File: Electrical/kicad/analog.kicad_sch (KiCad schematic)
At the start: 2 parts, among them IC2 PCM1795DBR

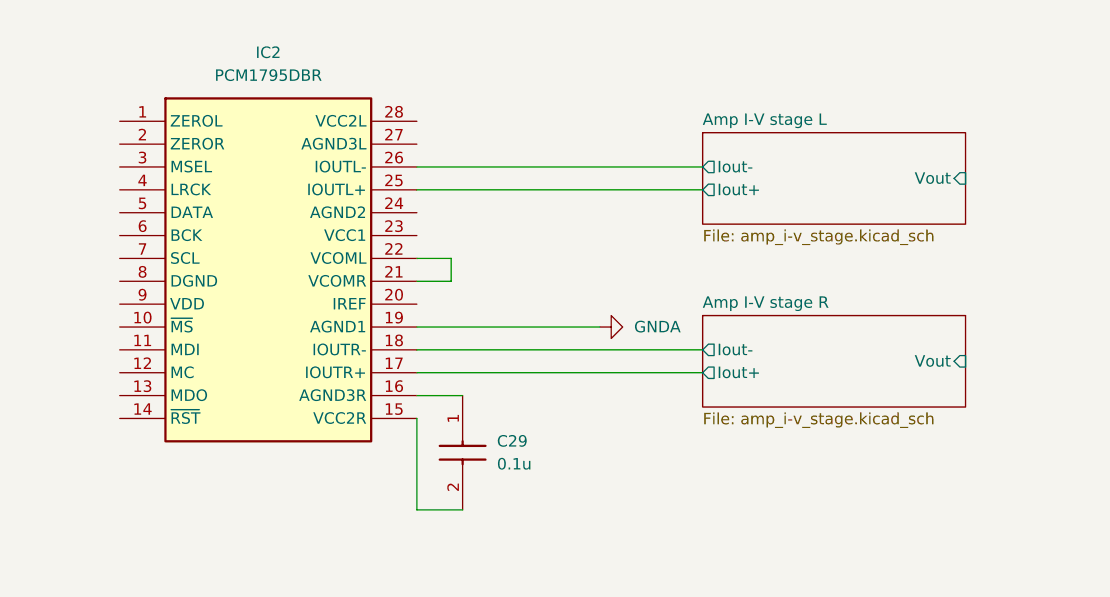
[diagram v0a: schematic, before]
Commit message: Updated PCM1795 schematic sheet
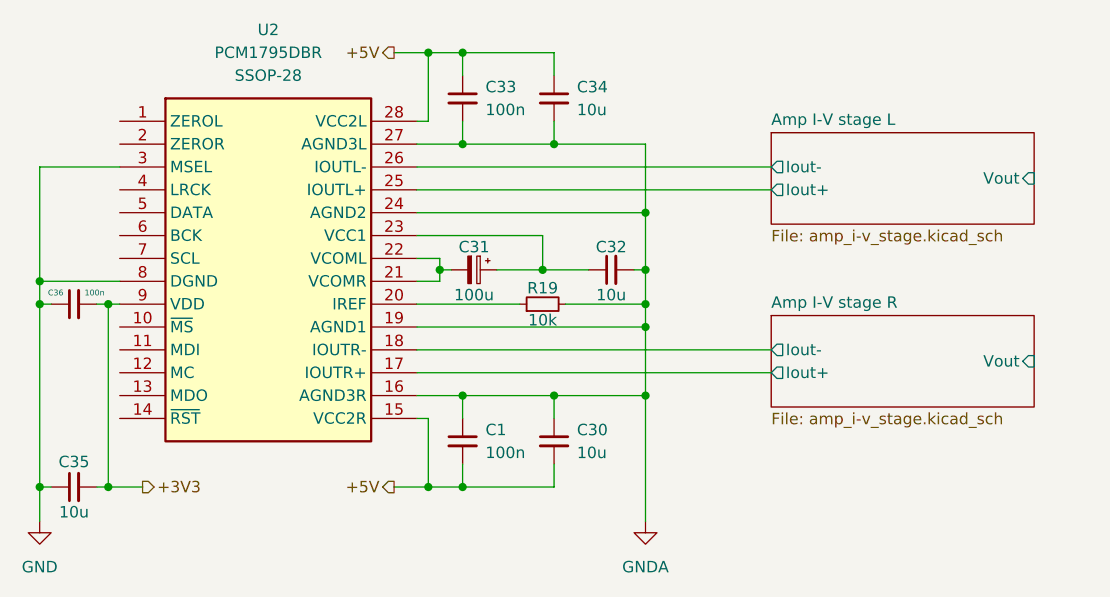
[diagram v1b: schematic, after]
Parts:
- removed C29: 0.1u, PHE426HJ6100JR05, symbol Project_Library:PHE426HJ6100JR05
- removed IC2: PCM1795DBR, SOP65P780X200-28N, symbol Project_Library:PCM1795DBR
- added C1, C33, C36: 100n, Project_Library:PHE426HJ6100JR05, symbol Project_Library:C_100n
- added C30, C32, C34, C35: 10u, Project_Library:CAPC3225X270N, symbol Project_Library:C_10u
- added C31: 100u, Project_Library:CAPPRD350W60D825H1300, symbol Project_Library:C_100u
- added R19: 10k, Project_Library:ERA6AEB101V, symbol Project_Library:R_10k
- added U2: PCM1795DBR, Project_Library:SOP65P780X200-28N, symbol Project_Library:U_PCM1795DBR
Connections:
- net Amp I-V stage L/Iout+: now also U2.25 (IOUTL+)
- net Amp I-V stage L/Iout-: now also U2.26 (IOUTL-)
- net Amp I-V stage R/Iout+: now also U2.17 (IOUTR+)
- net Amp I-V stage R/Iout-: now also U2.18 (IOUTR-)
- net GNDA: now also C1.1, C30.1, C32.2, C33.2, C34.2, R19.2, U2.16 (AGND3R), U2.19 (AGND1), U2.24 (AGND2), U2.27 (AGND3L)
- new net: R19.1, U2.20 (IREF)
- new net: C31.2, U2.21 (VCOMR), U2.22 (VCOML)
- new net: C31.1, C32.1, U2.23 (VCC1)
- new net +3V3: C35.2, C36.2, U2.9 (VDD)
- new net +5V: C1.2, C30.2, C33.1, C34.1, U2.15 (VCC2R), U2.28 (VCC2L)
- new net GND: C35.1, C36.1, U2.3 (MSEL), U2.8 (DGND)
